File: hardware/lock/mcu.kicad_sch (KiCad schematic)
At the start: 13 parts, among them J2 I2C JST-PH RA, J4 UPDI PROG, J6 HALL DOOR, J7 HALL BOLT, U1 ATtiny1616

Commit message: lock: power from I2C connector (VSYS), LED on PC3; route board; ephemerkey J2=VSYS
Power move: the lock has NO local battery (J1 removed) — VCC and the boost/
actuator draw come from ephemerkey's VSYS rail over the I2C connector (J2.2).
- ephemerkey: J2.2 = VSYS (was +3V3); manifest note + DESIGN.md updated, regenerated.
- lock: README interface/architecture/BOM + servo source (R13=VSOL / R14=VSYS,
  no more VBAT) updated to match the as-wired board.
- Caveat documented: a 12V solenoid pull-in (~3-4A) exceeds a JST-PH contact and
  ephemerkey's load-share; favor the 6V servo / low-duty, or a dedicated feed.
- I2C pull-ups stay on ephemerkey at +3V3 (STM32 pins not >3.6V tolerant).

LED move: status LED (D1) is driven by PC3, not PA3 (PA3 now spare). Docs + manifest.

lock schematic + PCB are now hand-wired and fully routed (DRC: 0 unconnected,
0 schematic-parity). Manifest marked REFERENCE-OF-RECORD — do not regenerate
(would destroy the wiring). Verified with KiCad's own kicad-cli ERC/DRC.

Pending (owner fixing): PWR_FLAGs on VCC/GND, NC flags on unused pins, J6/J7 GND
thermal relief, minor stub/silk cleanups.

Co-Authored-By: Claude Opus 4.8 (1M context) <noreply@anthropic.com>
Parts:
- U1: footprint Package_DFN_QFN:QFN-20-1EP_3x3mm_P0.4mm_EP1.65x1.65mm -> Package_DFN_QFN:VQFN-20-1EP_3x3mm_P0.4mm_EP1.7x1.7mm; LCSC C507118 -> (none); MPN ATTINY1616-MNR -> (none); Manufacturer Microchip -> (none)
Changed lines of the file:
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@@
+	)
+	(junction
+		(at 36.83 52.07)
+		(diameter 0)
+		(color 0 0 0 0)
 	)
 	(junction
@@
 	(wire
 		(pts
-			(xy 36.83 50.8) (xy 36.83 53.34)
+			(xy 36.83 50.8) (xy 36.83 52.07)
 		)
 		(stroke
@@
 	(wire
 		(pts
+			(xy 36.83 52.07) (xy 36.83 53.34)
+		)
+		(stroke
+			(width 0)
+			(type default)
+		)
+	)
+	(wire
+		(pts
 			(xy 125.73 96.52) (xy 135.89 96.52)
 		)
@@
 	(wire
 		(pts
+			(xy 27.94 52.07) (xy 36.83 52.07)
+		)
+		(stroke
+			(width 0)
+			(type default)
+		)
+	)
+	(wire
+		(pts
 			(xy 101.6 86.36) (xy 109.22 86.36)
 		)
@@
 		(pts
 			(xy 152.4 135.89) (xy 152.4 137.16)
+		)
+		(stroke
+			(width 0)
+			(type default)
+		)
+	)
+	(wire
+		(pts
+			(xy 27.94 50.8) (xy 27.94 52.07)
 		)
 		(stroke
@@
 	(label "SDA"
 		(at 138.43 74.93 0)
-		(effects
-			(font
-				(size 1.27 1.27)
-			)
-			(justify left bottom)
-		)
-	)
-	(label "HAL_DOOR"
-		(at 3.81 27.94 0)
 		(effects
 			(font
@@
 			)
 		)
-		(property "Footprint" "Package_DFN_QFN:QFN-20-1EP_3x3mm_P0.4mm_EP1.65x1.65mm"
+		(property "Footprint" "Package_DFN_QFN:VQFN-20-1EP_3x3mm_P0.4mm_EP1.7x1.7mm"
 			(at 86.36 73.66 0)
 			(hide yes)
@@
 				(font
 					(size 1.27 1.27)
-				)
-			)
-		)
-		(property "Datasheet" "~"
+					(italic yes)
+				)
+			)
+		)
+		(property "Datasheet" "http://ww1.microchip.com/downloads/en/DeviceDoc/ATtiny3216_ATtiny1616-data-sheet-40001997B.pdf"
 			(at 86.36 73.66 0)
 			(hide yes)
@@
 			)
 		)
-		(property "Description" ""
-			(at 86.36 73.66 0)
-			(show_name no)
-			(do_not_autoplace no)
-			(effects
-				(font
-					(size 1.27 1.27)
-				)
-			)
-		)
-		(property "LCSC" "C507118"
-			(at 86.36 73.66 0)
-			(hide yes)
-			(show_name no)
-			(do_not_autoplace no)
-			(effects
-				(font
-					(size 1.27 1.27)
-				)
-			)
-		)
-		(property "MPN" "ATTINY1616-MNR"
-			(at 86.36 73.66 0)
-			(hide yes)
-			(show_name no)
-			(do_not_autoplace no)
-			(effects
-				(font
-					(size 1.27 1.27)
-				)
-			)
-		)
-		(property "Manufacturer" "Microchip"
+		(property "Description" "20MHz, 16kB Flash, 2kB SRAM, 256B EEPROM, VQFN-20"
 			(at 86.36 73.66 0)
 			(hide yes)
@@
 					(unit 1)
 				)
+			)
+		)
+	)
+	(symbol
+		(lib_id "power:PWR_FLAG")
+		(at 27.94 50.8 0)
+		(unit 1)
+		(body_style 1)
+		(exclude_from_sim no)
+		(in_bom yes)
+		(on_board yes)
+		(in_pos_files yes)
+		(dnp no)
+		(fields_autoplaced yes)
+		(property "Reference" "#FLG02"
+			(at 27.94 48.895 0)
+			(hide yes)
+			(show_name no)
+			(do_not_autoplace no)
+			(effects
+				(font
+					(size 1.27 1.27)
+				)
+			)
+		)
+		(property "Value" "PWR_FLAG"
+			(at 27.94 45.72 0)
+			(show_name no)
+			(do_not_autoplace no)
+			(effects
+				(font
+					(size 1.27 1.27)
+				)
+			)
+		)
+		(property "Footprint" ""
+			(at 27.94 50.8 0)
+			(hide yes)
+			(show_name no)
+			(do_not_autoplace no)
+			(effects
+				(font
+					(size 1.27 1.27)
+				)
+			)
+		)
+		(property "Datasheet" ""
+			(at 27.94 50.8 0)
+			(hide yes)
+			(show_name no)
+			(do_not_autoplace no)
+			(effects
+				(font
+					(size 1.27 1.27)
+				)
+			)
+		)
+		(property "Description" "Special symbol for telling ERC where power comes from"
+			(at 27.94 50.8 0)
+			(hide yes)
+			(show_name no)
+			(do_not_autoplace no)
+			(effects
+				(font
+					(size 1.27 1.27)
+				)
+			)
+		)
+		(pin "1"
+		)
+		(instances
+			(project "lock"
+				(path "/e1000000-0000-4000-8000-000000000002/9796a12a-a53a-47bc-9480-fd5121fe7c15"
+					(reference "#FLG02")
+					(unit 1)
+				)

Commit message: lock: restore U1 (ATtiny1616) LCSC/MPN — C507118 / ATTINY1616-MNR
U1 lost its LCSC/MPN/Manufacturer fields when re-placed from the KiCad
library; without them JLCPCB assembly can't source the MCU. Re-added so the
assembly BOM matches the part.

Co-Authored-By: Claude Opus 4.8 (1M context) <noreply@anthropic.com>
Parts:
- U1: LCSC (none) -> C507118; MPN (none) -> ATTINY1616-MNR; Manufacturer (none) -> Microchip
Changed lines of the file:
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@@
+			)
+		)
+		(property "LCSC" "C507118"
+			(at 86.36 73.66 0)
+			(hide yes)
+			(show_name no)
+			(do_not_autoplace no)
+			(effects
+				(font
+					(size 1.27 1.27)
+				)
+			)
+		)
+		(property "MPN" "ATTINY1616-MNR"
+			(at 86.36 73.66 0)
+			(hide yes)
+			(show_name no)
+			(do_not_autoplace no)
+			(effects
+				(font
+					(size 1.27 1.27)
+				)
+			)
+		)
+		(property "Manufacturer" "Microchip"
+			(at 86.36 73.66 0)
+			(hide yes)
+			(show_name no)
+			(do_not_autoplace no)
+			(effects
+				(font
+					(size 1.27 1.27)
+				)
 			)
 		)

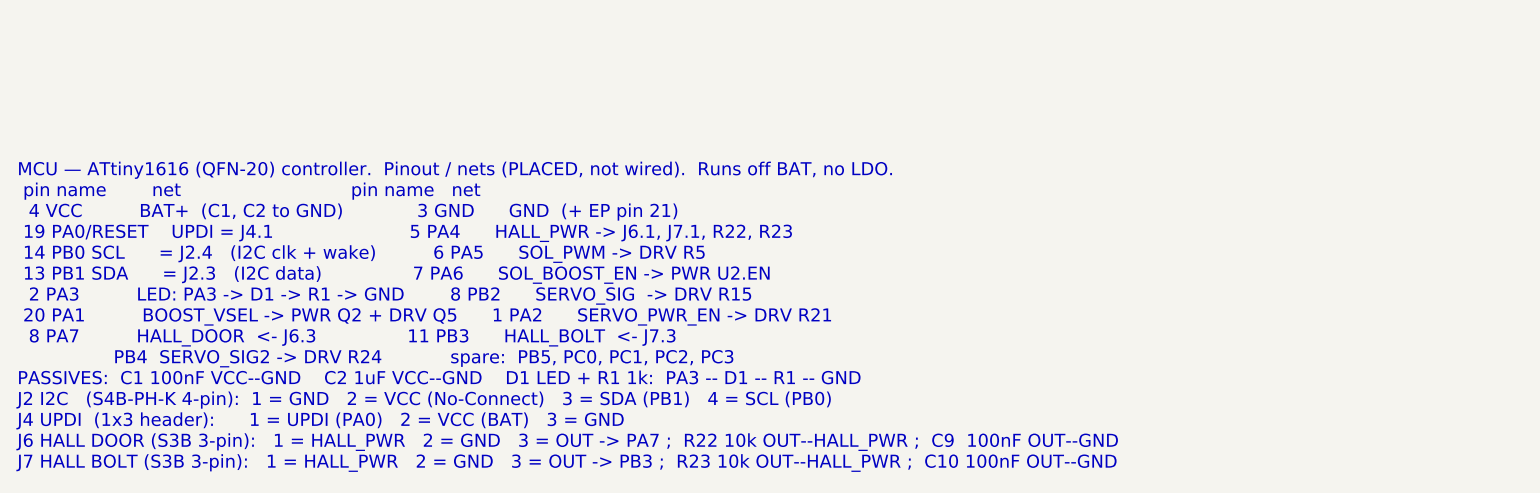
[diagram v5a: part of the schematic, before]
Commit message: hardware: fix PSU load-share S/D, make all sheet notes monospace
The PSU wiring note specified Q1 (AO3401A load-share PMOS) as S=BAT+,
D=VSYS. A PMOS body diode conducts D->S, so that orientation points the
diode VSYS -> BAT+: with USB attached VSYS sits ~4.7V (VBUS - D3) against
a 3.0-4.2V cell, forward-biasing it and dumping uncontrolled current into
the battery, bypassing the MCP73831 charger entirely.

Correct assignment is D=BAT+, S=VSYS, so the body diode points BAT+ ->
VSYS: the battery always reaches the load, and USB can never back-feed
the cell. Q1 was placed but never wired (all three pins are unconnected
in the netlist), so this is a spec fix ahead of wiring, not a board
change. The lock's Q3 is a high-side switch and deliberately uses the
opposite S/D assignment; the note now says so, to stop the two being
"reconciled" by pattern-matching.

Also relaid the PSU note as a two-column table and gave every sheet note
the Courier New face the generator already emits (kschgen NOTE_FONT, added
in 43a6067). The sheets predate that commit, so their notes rendered in
KiCad's variable-width stroke font and the space-padded pin tables did not
line up. Font only on the other six notes -- text is untouched.

Verified: kicad-cli netlists for both boards are byte-identical before and
after (ephemerkey 259 nodes, lock 131 nodes) once the export timestamp is
excluded; no non-font lines changed in any sheet; all sheets re-rendered
and the notes fit inside the page frame.

The four ephemerkey sheets also carry pre-existing eeschema reformatting
(expanded lib_symbols) that was already in the working tree.

Co-Authored-By: Claude Opus 4.8 (1M context) <noreply@anthropic.com>
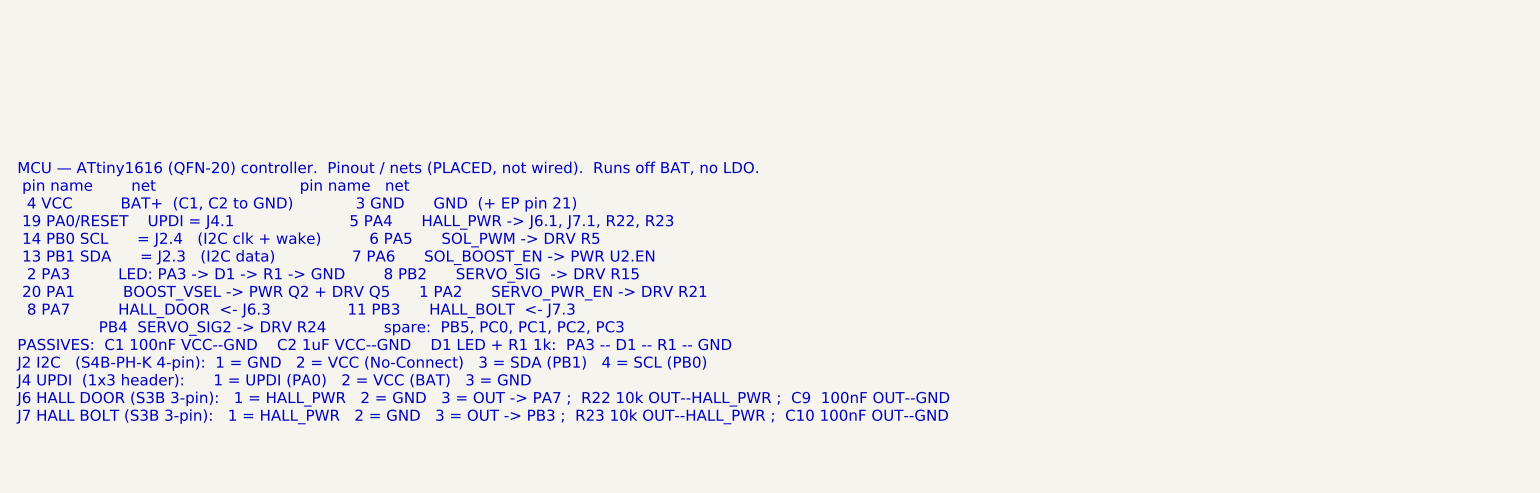
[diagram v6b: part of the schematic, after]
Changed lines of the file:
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@@
 		(effects
 			(font
-				(size 1.5 1.5)
+				(face "Courier New")
+				(size 1.27 1.27)
 			)
 			(justify left top)

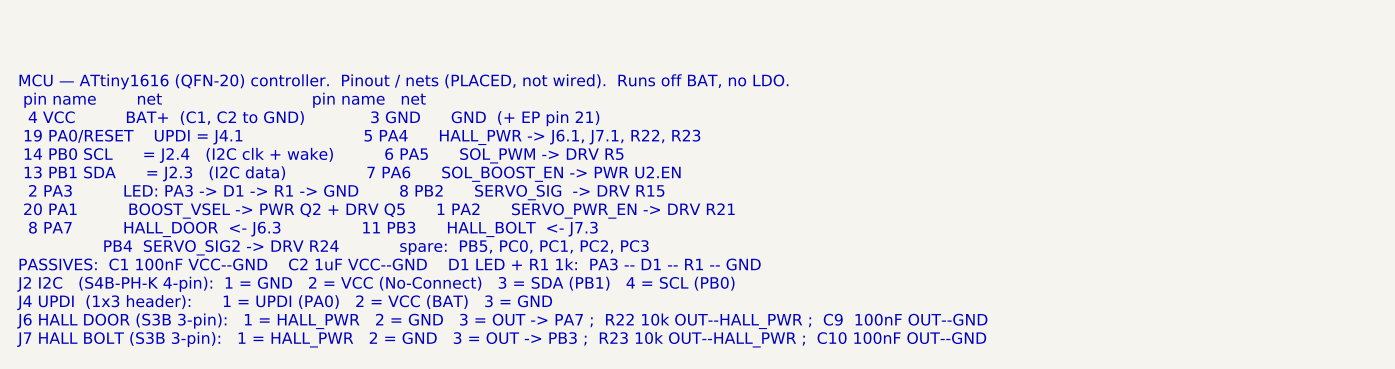
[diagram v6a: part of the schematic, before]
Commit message: hardware: gate OLED/EEPROM/I2C1 pull-ups behind PERI_EN load switch
Free the LIS3DH 2nd interrupt pin (tamper/free-fall now OR'd onto INT1 via
CTRL_REG3 I1_IA2) and repurpose it as PERI_EN. Add a high-side load switch on
the Sensors sheet (Q3 AO3401A pass FET, Q4 AO3400A gate driver, R30/R31 100k,
C31 1uF) powering a new +3V3_SW rail for DS1 OLED, U7 EEPROM, and the I2C1
pull-ups R9/R10 -- all gated off in Stop so they don't leak. LIS3DH stays on
always-on +3V3 as the wake source; FW drives PB6/PB7 low before Stop so the
powered accel never floats on the unpulled bus.

Surgical edits to both the .kicad_sch sheets and the schgen manifests (no
regen -- sheets are already partially wired). PARTS.md updated (also fills the
previously-missing Q2 AO3400A row). Also fix the lock J2 note: pin 2 = VCC <-
ephemerkey VSYS (was mislabeled "No-Connect", contradicting the wired net).

Co-Authored-By: Claude Opus 4.8 (1M context) <noreply@anthropic.com>
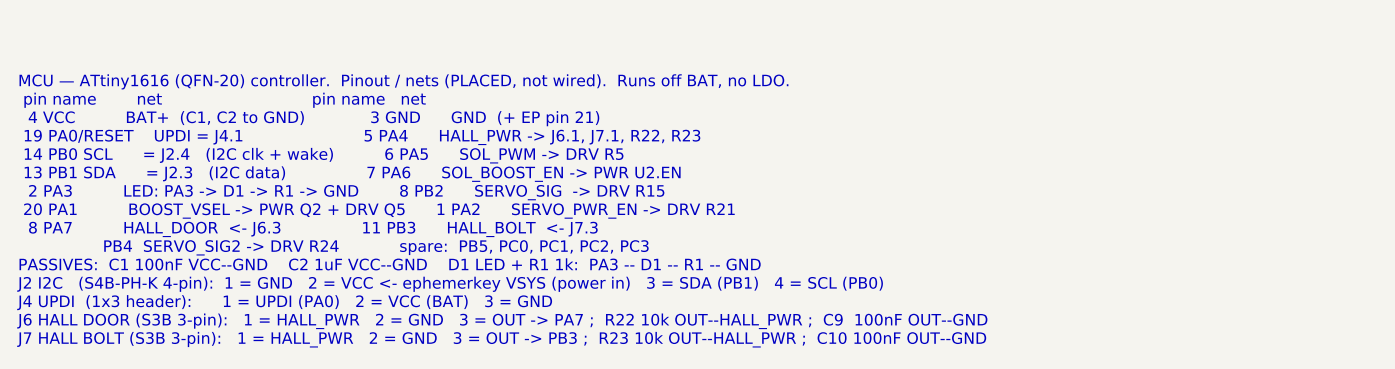
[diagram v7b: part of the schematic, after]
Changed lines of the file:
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@@
 		(company "EphemerKey Authors")
 	)
-	(text "MCU — ATtiny1616 (QFN-20) controller.  Pinout / nets (PLACED, not wired).  Runs off BAT, no LDO.\n pin name        net                              pin name   net\n  4 VCC          BAT+  (C1, C2 to GND)             3 GND      GND  (+ EP pin 21)\n 19 PA0/RESET    UPDI = J4.1                        5 PA4      HALL_PWR -> J6.1, J7.1, R22, R23\n 14 PB0 SCL      = J2.4   (I2C clk + wake)          6 PA5      SOL_PWM -> DRV R5\n 13 PB1 SDA      = J2.3   (I2C data)                7 PA6      SOL_BOOST_EN -> PWR U2.EN\n  2 PA3          LED: PA3 -> D1 -> R1 -> GND        8 PB2      SERVO_SIG  -> DRV R15\n 20 PA1          BOOST_VSEL -> PWR Q2 + DRV Q5      1 PA2      SERVO_PWR_EN -> DRV R21\n  8 PA7          HALL_DOOR  <- J6.3                11 PB3      HALL_BOLT  <- J7.3\n                 PB4  SERVO_SIG2 -> DRV R24            spare:  PB5, PC0, PC1, PC2, PC3\nPASSIVES:  C1 100nF VCC--GND    C2 1uF VCC--GND    D1 LED + R1 1k:  PA3 -- D1 -- R1 -- GND\nJ2 I2C   (S4B-PH-K 4-pin):  1 = GND   2 = VCC (No-Connect)   3 = SDA (PB1)   4 = SCL (PB0)\nJ4 UPDI  (1x3 header):      1 = UPDI (PA0)   2 = VCC (BAT)   3 = GND\nJ6 HALL DOOR (S3B 3-pin):   1 = HALL_PWR   2 = GND   3 = OUT -> PA7 ;  R22 10k OUT--HALL_PWR ;  C9  100nF OUT--GND\nJ7 HALL BOLT (S3B 3-pin):   1 = HALL_PWR   2 = GND   3 = OUT -> PB3 ;  R23 10k OUT--HALL_PWR ;  C10 100nF OUT--GND"
+	(text "MCU — ATtiny1616 (QFN-20) controller.  Pinout / nets (PLACED, not wired).  Runs off BAT, no LDO.\n pin name        net                              pin name   net\n  4 VCC          BAT+  (C1, C2 to GND)             3 GND      GND  (+ EP pin 21)\n 19 PA0/RESET    UPDI = J4.1                        5 PA4      HALL_PWR -> J6.1, J7.1, R22, R23\n 14 PB0 SCL      = J2.4   (I2C clk + wake)          6 PA5      SOL_PWM -> DRV R5\n 13 PB1 SDA      = J2.3   (I2C data)                7 PA6      SOL_BOOST_EN -> PWR U2.EN\n  2 PA3          LED: PA3 -> D1 -> R1 -> GND        8 PB2      SERVO_SIG  -> DRV R15\n 20 PA1          BOOST_VSEL -> PWR Q2 + DRV Q5      1 PA2      SERVO_PWR_EN -> DRV R21\n  8 PA7          HALL_DOOR  <- J6.3                11 PB3      HALL_BOLT  <- J7.3\n                 PB4  SERVO_SIG2 -> DRV R24            spare:  PB5, PC0, PC1, PC2, PC3\nPASSIVES:  C1 100nF VCC--GND    C2 1uF VCC--GND    D1 LED + R1 1k:  PA3 -- D1 -- R1 -- GND\nJ2 I2C   (S4B-PH-K 4-pin):  1 = GND   2 = VCC <- ephemerkey VSYS (power in)   3 = SDA (PB1)   4 = SCL (PB0)\nJ4 UPDI  (1x3 header):      1 = UPDI (PA0)   2 = VCC (BAT)   3 = GND\nJ6 HALL DOOR (S3B 3-pin):   1 = HALL_PWR   2 = GND   3 = OUT -> PA7 ;  R22 10k OUT--HALL_PWR ;  C9  100nF OUT--GND\nJ7 HALL BOLT (S3B 3-pin):   1 = HALL_PWR   2 = GND   3 = OUT -> PB3 ;  R23 10k OUT--HALL_PWR ;  C10 100nF OUT--GND"
 		(exclude_from_sim no)
 		(at 21.336 179.07 0)
